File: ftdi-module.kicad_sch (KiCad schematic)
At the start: 46 parts

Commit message: Updated schematic
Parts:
- added C?: C_10u_16V_0603, d1600e-psu-breakout-board-footprints:0603-cap, symbol d1600e-psu-breakout-board:C_10u_25V_0603
- added C? (x2): C_22u_0603, d1600e-psu-breakout-board-footprints:0603-cap, symbol d1600e-psu-breakout-board:C_22u_0603
- added C?: C_100n_0402, d1600e-psu-breakout-board-footprints:0402-cap, symbol d1600e-psu-breakout-board:C_100n_0402
- added FB?: BLM21SN300SZ1D, antmicro-footprints:FB_0805_2012Metric, symbol antmicroFerriteBeadsandChips:BLM21SN300SZ1D
- added L?: 74437336033, d1600e-psu-breakout-board-footprints:WE_74437336033, symbol d1600e-psu-breakout-board:74437336033
- added R?: R_680R_0402, antmicro-footprints:0402-res, symbol antmicroResistors0402:R_680R_0402
- added R?: R_2k15_0402, antmicro-footprints:0402-res, symbol antmicroResistors0402:R_2k15_0402
- added U?: LM1117MP-25NOPB, antmicro-footprints:SOT-223, symbol antmicroPMICVoltageRegulatorsLinear:LM1117MP-25NOPB
- added U?: AP62301WU-7, d1600e-psu-breakout-board-footprints:TSOT23-6, symbol d1600e-psu-breakout-board:AP62301WU-7
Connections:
- net GND: now also C?.2, C?.2, C?.2, R?.2, U?.1 (GND)
- net VCC12V0: now also C?.1, U?.3 (VIN)
- new net: C?.1, C?.1, FB?.1, L?.2 (P), R?.1
- new net: C?.1, L?.1 (P), U?.2 (SW)
- new net: U?.2 (VOUT), U?.4 (VOUT)
- new net: R?.1, R?.2, U?.4 (FB)
- new net: C?.2, U?.6 (BST)
- new net VCC5V0: FB?.2
- no-connect marks 34 -> 35
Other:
- note added: "5V0 DC/DC Converter"
- note added: "replace with LDO"

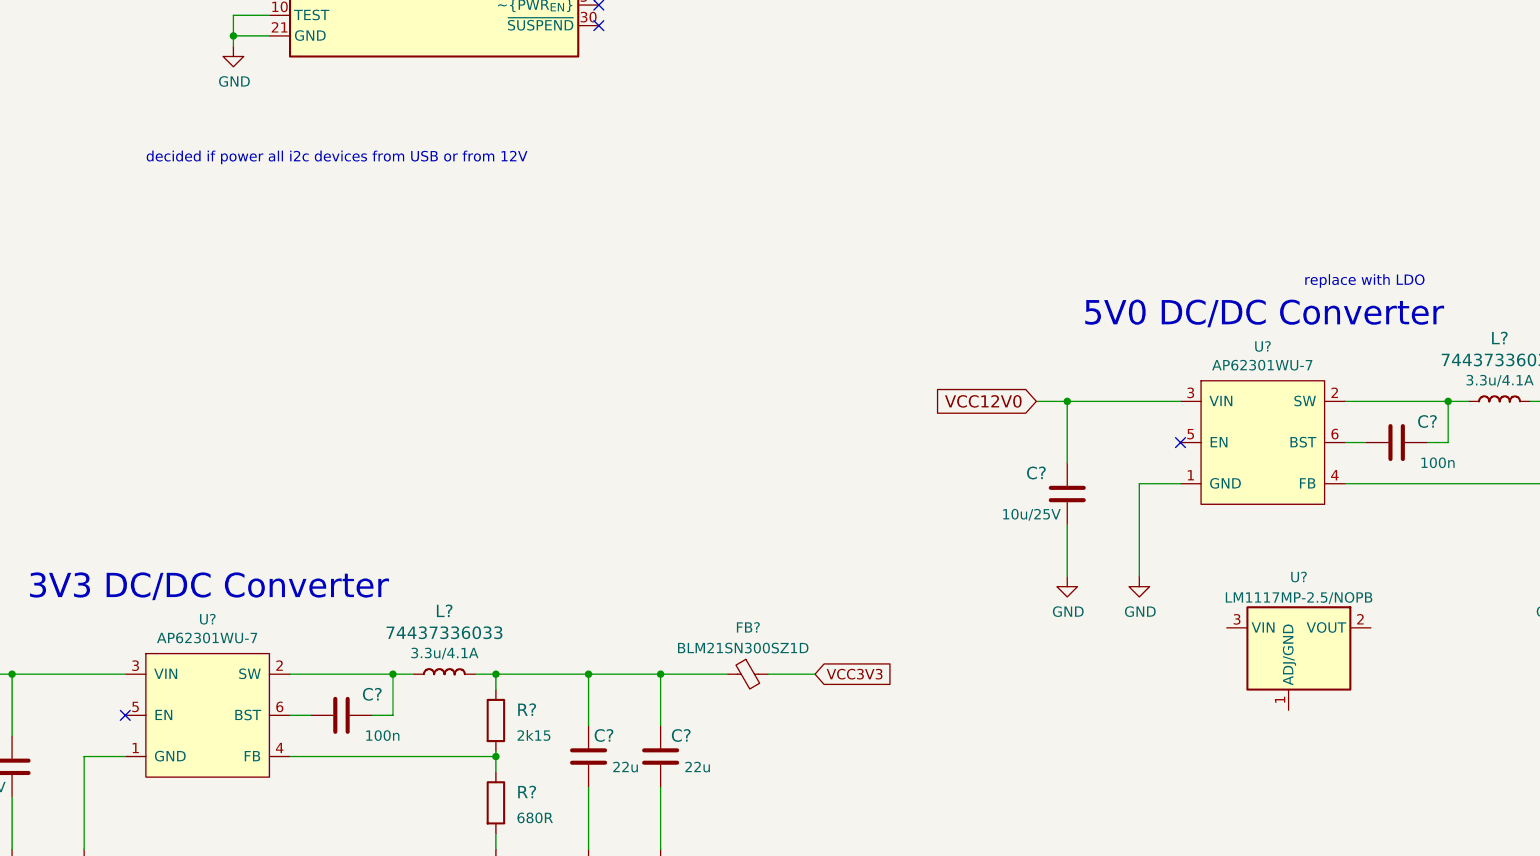
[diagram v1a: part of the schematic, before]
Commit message: Proposed arbiter for controlling fans
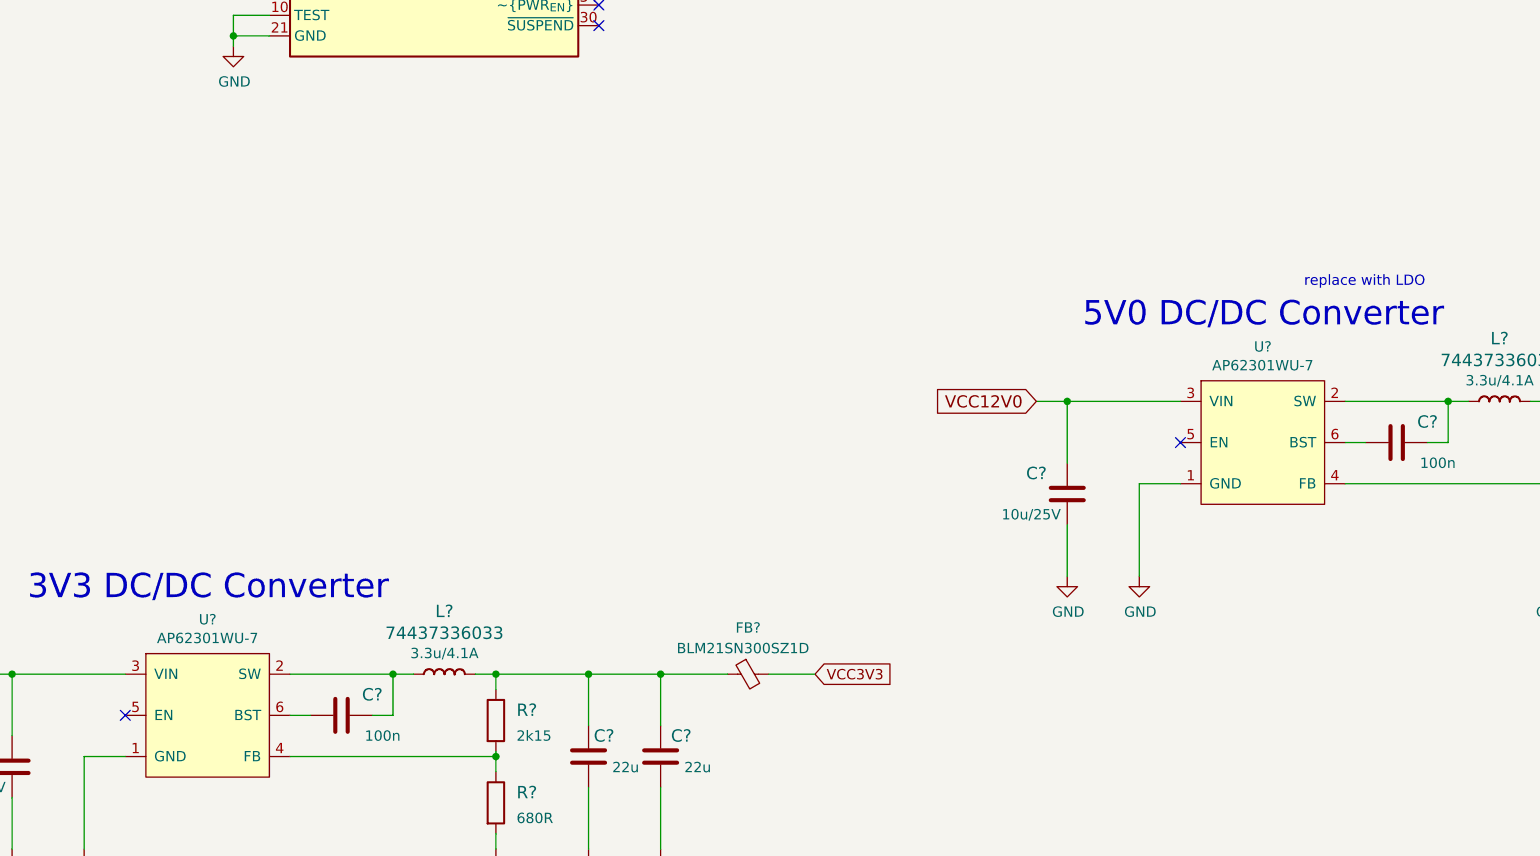
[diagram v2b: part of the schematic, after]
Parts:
- removed U?: LM1117MP-25NOPB, antmicro-footprints:SOT-223, symbol antmicroPMICVoltageRegulatorsLinear:LM1117MP-25NOPB
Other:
- note removed: "decided if power all i2c devices from USB or from 12V"
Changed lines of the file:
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@@
     (effects (font (size 2.9972 2.9972)) (justify left bottom))
-  )
-  (text "decided if power all i2c devices from USB or from 12V"
-    (at 179.705 182.88 0)
-    (effects (font (size 1.27 1.27)) (justify left bottom))
   )
   (text "5V0 DC/DC Converter" (at 295.275 203.2 0)
@@
     (pin "1")
   )
-  (symbol (lib_id "antmicroPMICVoltageRegulatorsLinear:LM1117MP-25NOPB") (at 313.055 240.03 0) (unit 1)
-    (in_bom yes) (on_board yes) (fields_autoplaced)
-    (property "Reference" "U?" (id 0) (at 321.945 233.805 0)
-      (effects (font (size 1.27 1.27) (thickness 0.15)))
-    )
-    (property "Value" "LM1117MP-25NOPB" (id 1) (at 346.075 247.65 0)
-      (effects (font (size 1.27 1.27) (thickness 0.15)) (justify left bottom) hide)
-    )
-    (property "Footprint" "antmicro-footprints:SOT-223" (id 2) (at 346.075 250.19 0)
-      (effects (font (size 1.27 1.27) (thickness 0.15)) (justify left bottom) hide)
-    )
-    (property "Datasheet" "https://www.ti.com/general/docs/suppproductinfo.tsp?distId=26&gotoUrl=https://www.ti.com/lit/gpn/lm1117" (id 3) (at 346.075 252.73 0)
-      (effects (font (size 1.27 1.27) (thickness 0.15)) (justify left bottom) hide)
-    )
-    (property "MPN" "LM1117MP-2.5/NOPB" (id 4) (at 321.945 236.3287 0)
-      (effects (font (size 1.27 1.27) (thickness 0.15)))
-    )
-    (property "Manufacturer" "Texas Instruments" (id 5) (at 346.075 255.27 0)
-      (effects (font (size 1.27 1.27) (thickness 0.15)) (justify left bottom) hide)
-    )
-    (property "Author" "Antmicro" (id 6) (at 346.075 257.81 0)
-      (effects (font (size 1.27 1.27) (thickness 0.15)) (justify left bottom) hide)
-    )
-    (property "License" "Apache-2.0" (id 7) (at 346.075 260.35 0)
-      (effects (font (size 1.27 1.27) (thickness 0.15)) (justify left bottom) hide)
-    )
-    (pin "1")
-    (pin "2")
-    (pin "3")
-    (pin "4")
-  )
   (symbol (lib_id "antmicroResonators:Resonator_12MHz_ABM8G") (at 160.02 130.175 0) (unit 1)

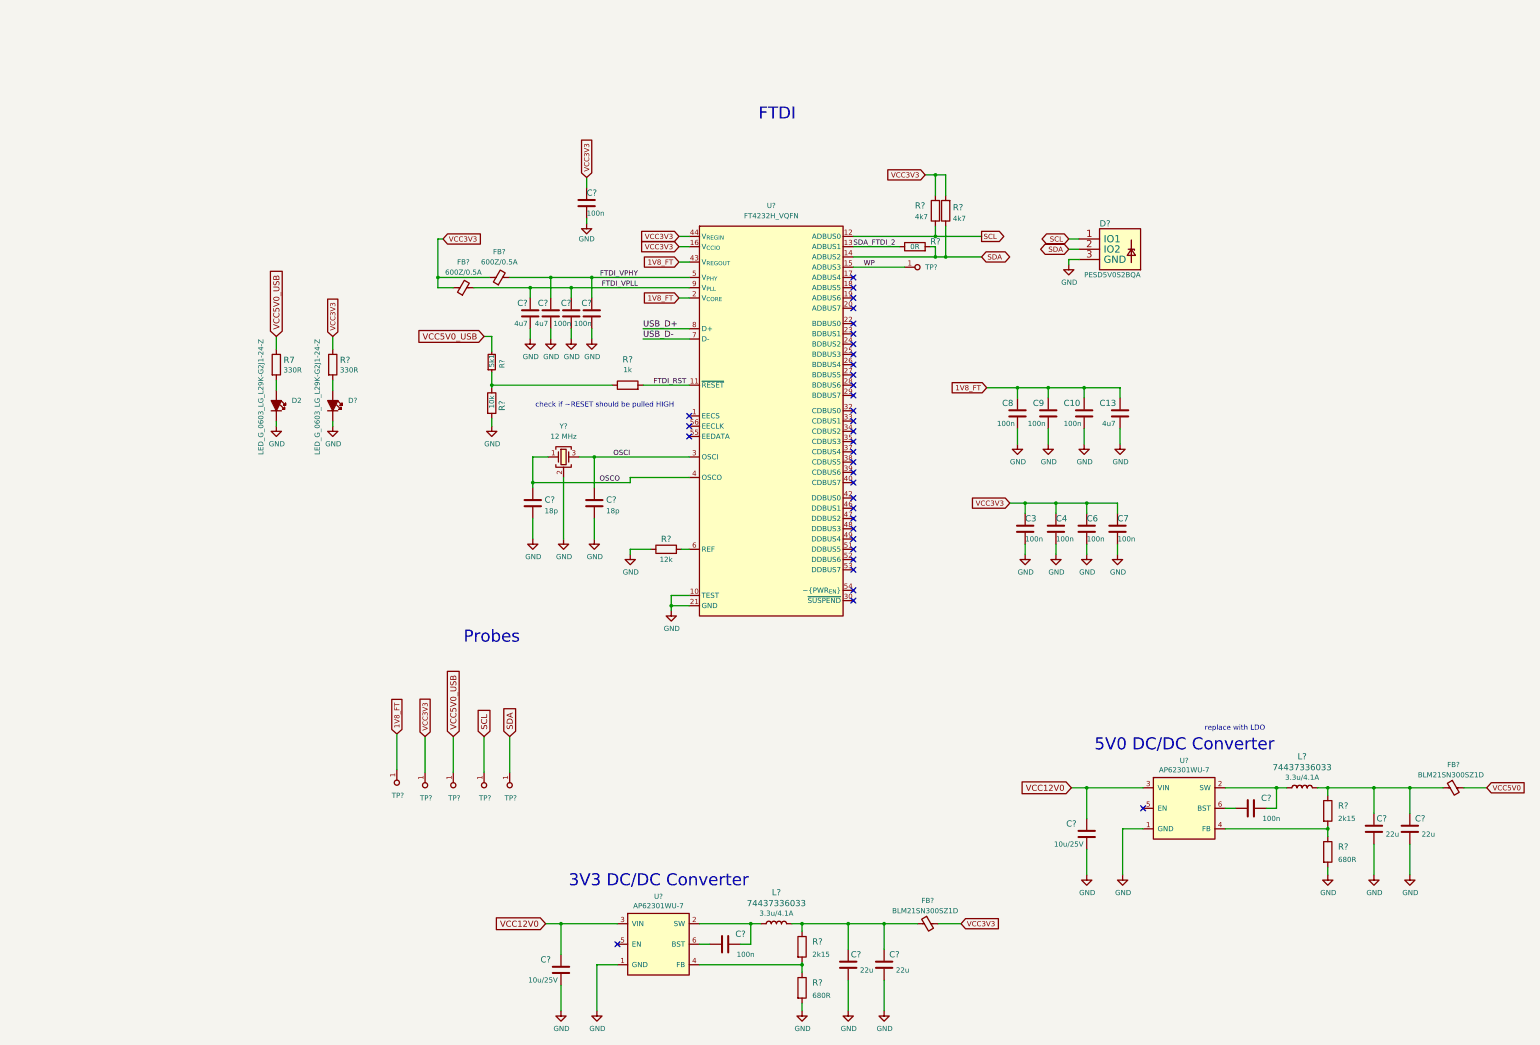
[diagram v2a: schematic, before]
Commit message: Rearange hierarchical schematics
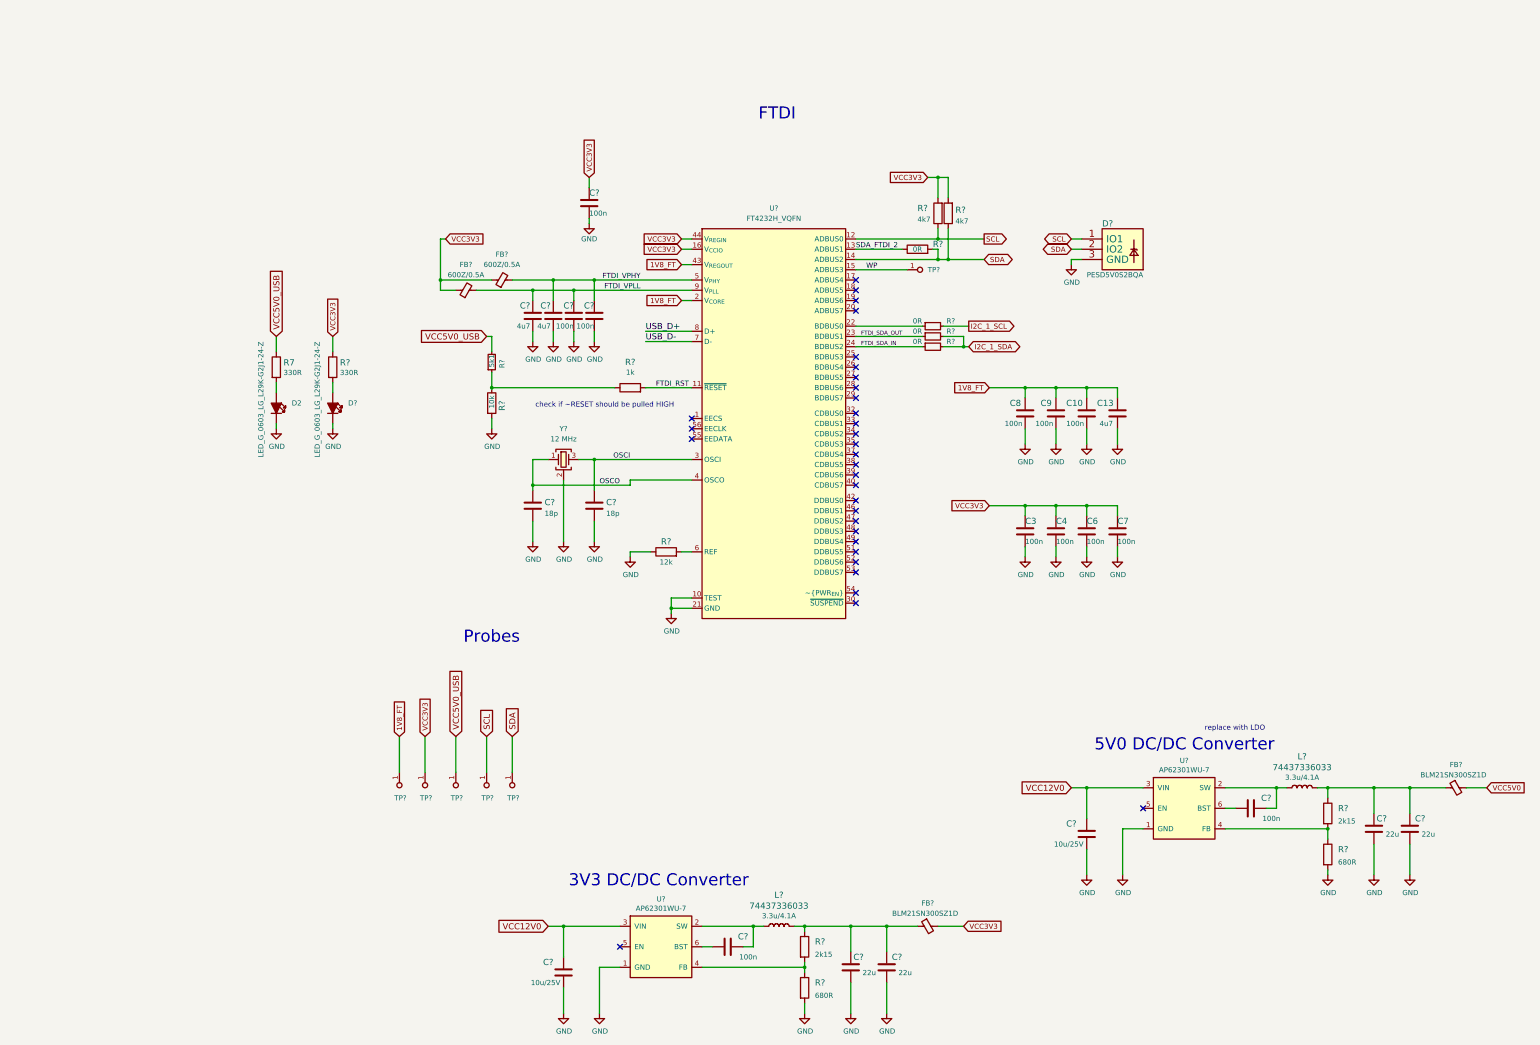
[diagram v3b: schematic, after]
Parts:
- added R? (x3): R_0R_0402, nuc-compute-cluster-environment-sensor-footprints:R_0402_1005Metric, symbol nuc-compute-cluster-environment-sensor:R_0R_0402
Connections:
- net at U?.22 (BDBUS0): now also R?.1
- net FTDI_SDA_OUT: now reaches U?.23 (BDBUS1)
- net FTDI_SDA_OUT: now also R?.1
- net FTDI_SDA_IN: now reaches U?.24 (BDBUS2)
- net FTDI_SDA_IN: now also R?.1
- new net I2C_1_SCL: R?.2
- new net I2C_1_SDA: R?.2, R?.2
- no-connect marks 35 -> 32
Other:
- moved on the sheet: C10, C13, C3, C4, C6, C7, C8, C9, C?, D2, D?, FB?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

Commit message: Mock placement of all components on schematic
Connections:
- net I2C_1_SCL is gone; now on net SCL: R?.2
- net I2C_1_SDA is gone; now on net SDA: R?.2, R?.2
- net VCC12V0 renamed 12V_INTERNAL
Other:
- note removed: "Probes"
- moved on the sheet: C10, C13, C3, C4, C6, C7, C8, C9, C?, D2, D?, FB?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
